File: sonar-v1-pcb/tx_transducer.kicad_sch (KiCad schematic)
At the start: 1 part

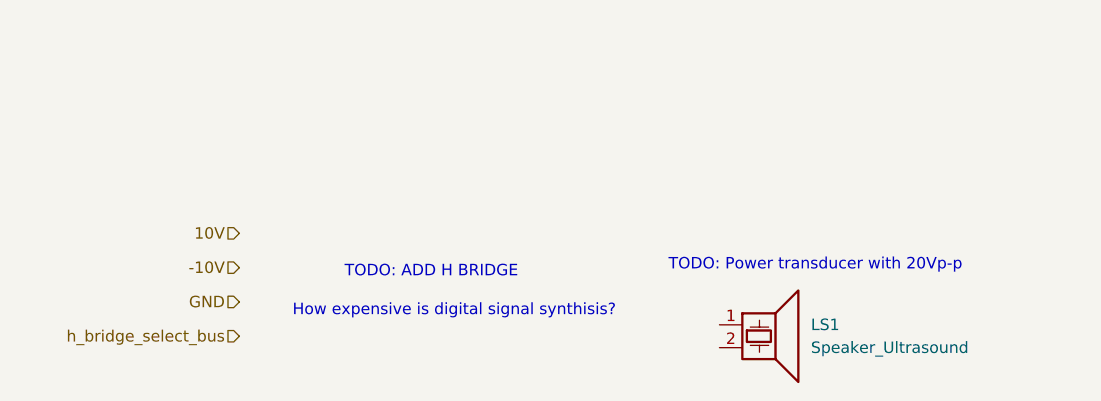
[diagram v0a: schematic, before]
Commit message: finish ADC signals
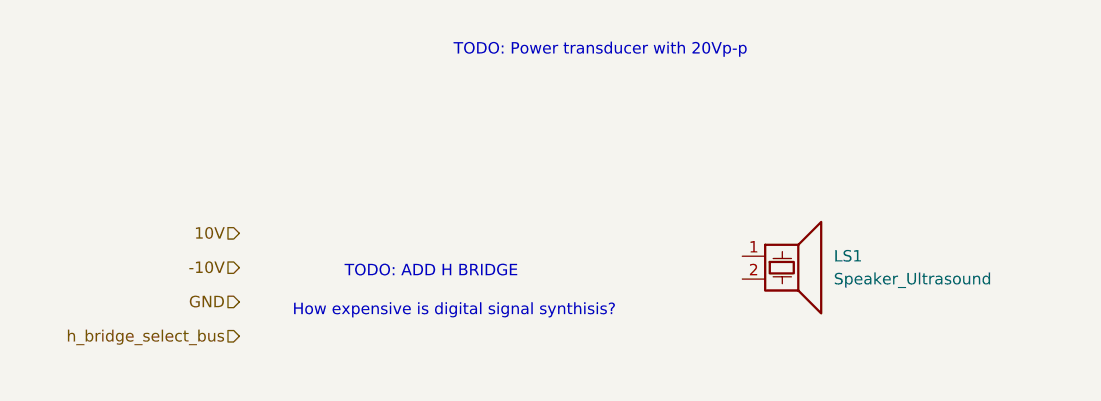
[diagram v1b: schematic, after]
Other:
- moved on the sheet: LS1
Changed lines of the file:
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@@
 	(text "TODO: Power transducer with 20Vp-p"
 		(exclude_from_sim no)
-		(at 110.998 91.186 0)
+		(at 87.122 67.31 0)
 		(effects
 			(font
@@
 	(symbol
 		(lib_id "Device:Speaker_Ultrasound")
-		(at 105.41 97.79 0)
+		(at 107.95 90.17 0)
 		(unit 1)
 		(exclude_from_sim no)
@@
 		(fields_autoplaced yes)
 		(property "Reference" "LS1"
-			(at 110.49 97.7899 0)
+			(at 113.03 90.1699 0)
 			(effects
 				(font
@@
 		)
 		(property "Value" "Speaker_Ultrasound"
-			(at 110.49 100.3299 0)
+			(at 113.03 92.7099 0)
 			(effects
 				(font
@@
 		)
 		(property "Footprint" "Sonar:MA40S4"
-			(at 104.521 99.06 0)
+			(at 107.061 91.44 0)
 			(effects
 				(font
@@
 		)
 		(property "Datasheet" "kicad-embed://ultrasonics.pdf"
-			(at 104.521 99.06 0)
+			(at 107.061 91.44 0)
 			(effects
 				(font
@@
 		)
 		(property "Description" "Ultrasonic transducer"
-			(at 105.41 97.79 0)
+			(at 107.95 90.17 0)
 			(effects
 				(font

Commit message: Switch to audio not just ultrasonic.
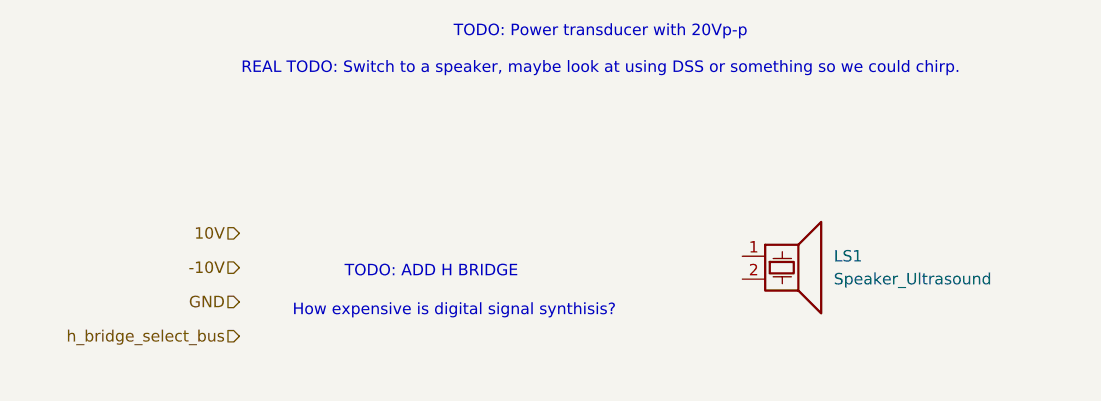
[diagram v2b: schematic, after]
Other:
- note added: "TODO: Power transducer with 20Vp-p REAL TODO: Switch to a speaker, maybe look at using DSS or something so we could chirp."
- note removed: "TODO: Power transducer with 20Vp-p"
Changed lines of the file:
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@@
 		)
 	)
-	(text "TODO: Power transducer with 20Vp-p"
+	(text "TODO: Power transducer with 20Vp-p\n\nREAL TODO: Switch to a speaker, maybe look at using DSS or something so we could chirp.\n"
 		(exclude_from_sim no)
 		(at 87.122 67.31 0)

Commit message: Josh cooking some more.
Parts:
- renumbered LS1 to LS3001
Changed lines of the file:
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@@
 		(dnp no)
 		(fields_autoplaced yes)
-		(property "Reference" "LS1"
+		(property "Reference" "LS3001"
 			(at 113.03 90.1699 0)
 			(effects
@@
 			)
 		)
-		(property "Datasheet" "kicad-embed://ultrasonics.pdf"
+		(property "Datasheet" "~"
 			(at 107.061 91.44 0)
 			(effects
@@
 			(project "sonar"
 				(path "/f72ceae0-eee4-4385-b0e8-639846bcb5f2/43b3c482-e2f0-4b6c-ae84-751c8208aa65"
-					(reference "LS1")
+					(reference "LS3001")
 					(unit 1)
 				)
